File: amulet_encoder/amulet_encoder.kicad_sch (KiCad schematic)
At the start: 42 parts, among them J7 SM07B-GHS-TB, Q7 PMV90ENER, U1 MA732GQ, U2 SN74AHC1G02DBVR

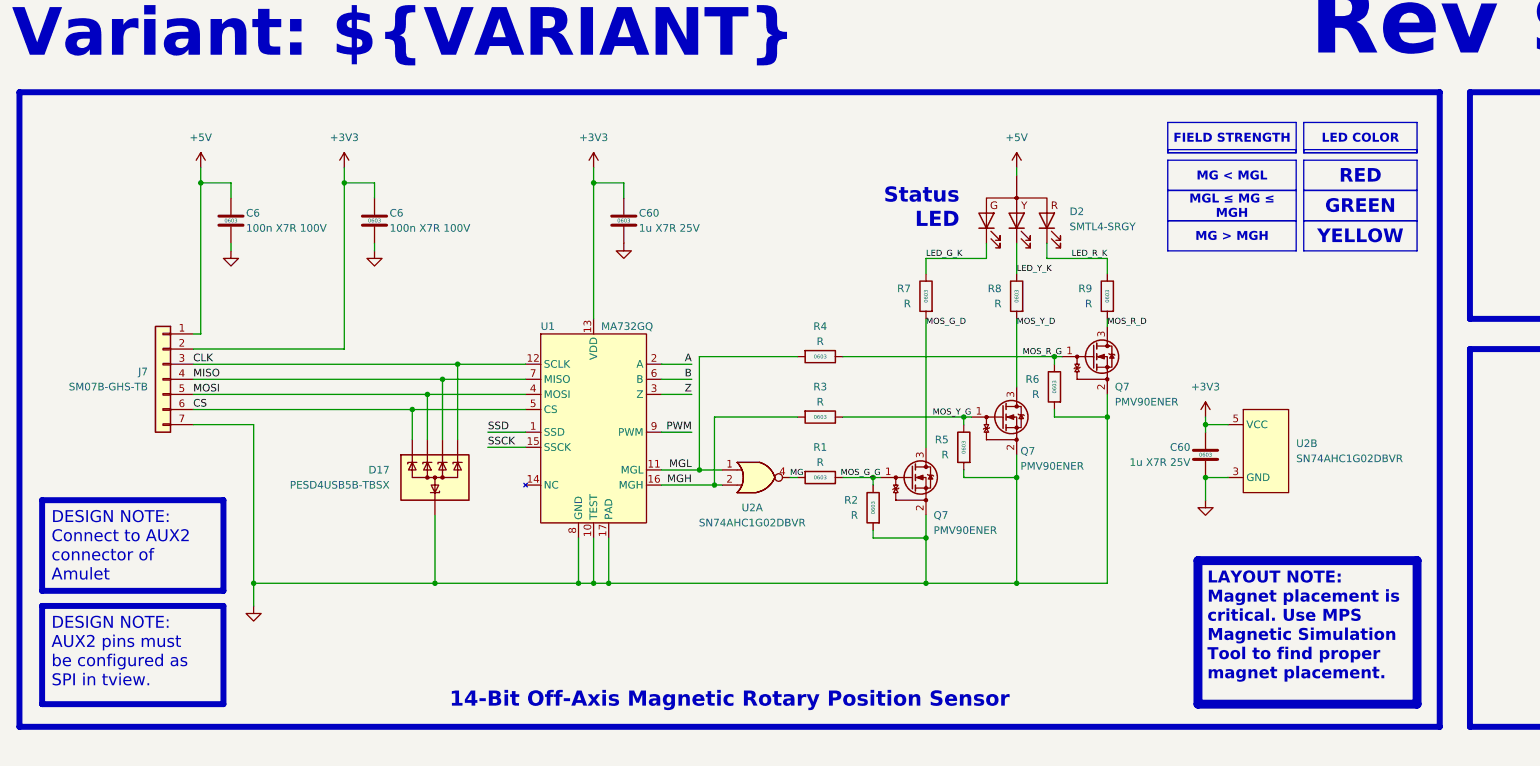
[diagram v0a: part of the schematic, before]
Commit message: preliminary layout
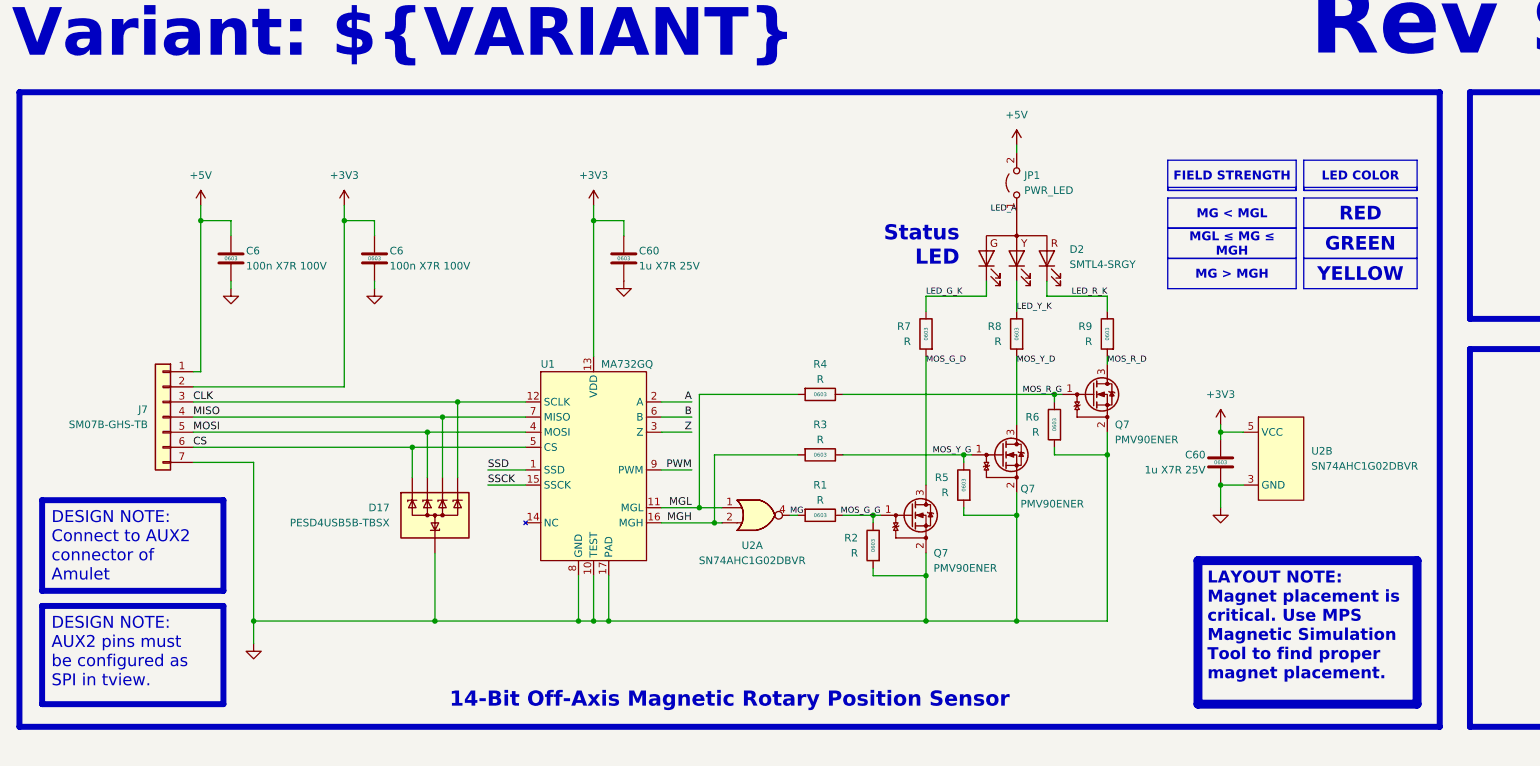
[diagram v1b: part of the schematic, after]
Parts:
- added JP1: PWR_LED, Jumper:SolderJumper-2_P1.3mm_Open_RoundedPad1.0x1.5mm, symbol Jumper:Jumper_2_Open
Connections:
- net +5V: now also JP1.2 (B); no longer D2.4 (A)
- new net LED_A: D2.4 (A), JP1.1 (A)
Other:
- moved on the sheet: C6, C60, D17, D2, J7, Q7, R1, R2, R3, R4, R5, R6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

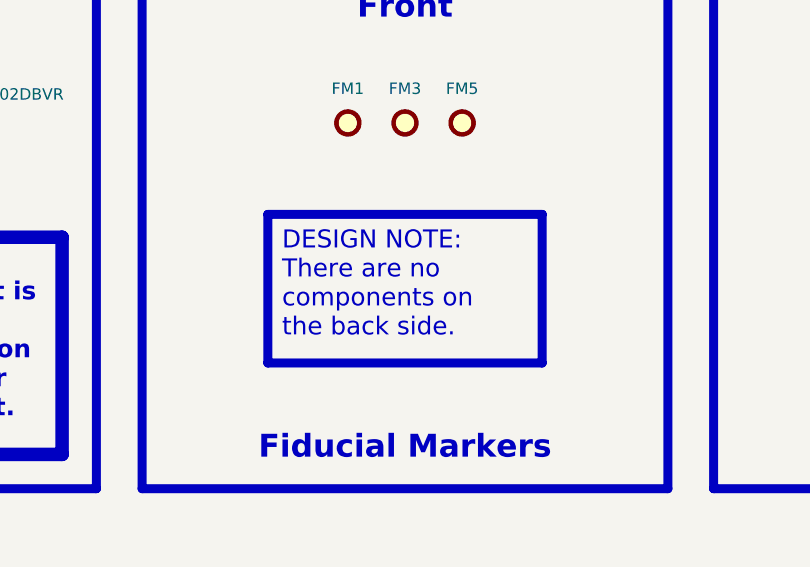
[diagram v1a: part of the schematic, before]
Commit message: preliminary routing of encoder
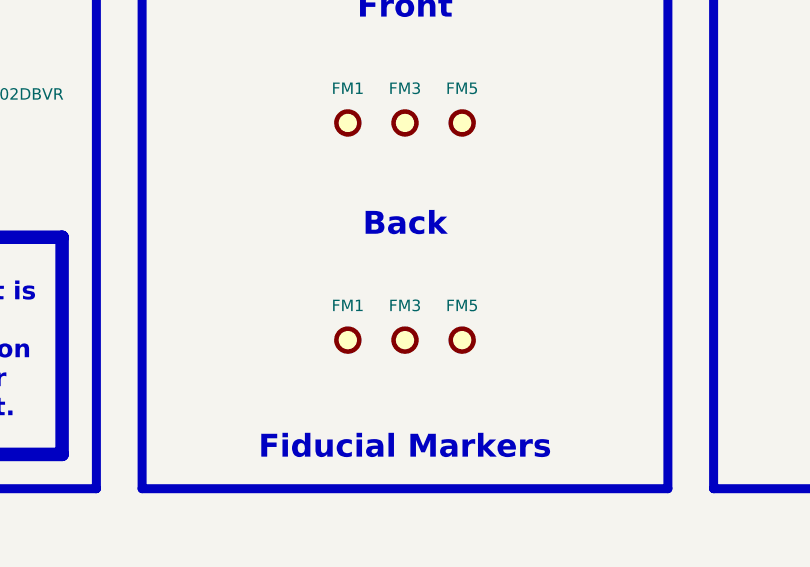
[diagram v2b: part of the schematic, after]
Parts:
- added FM1, FM3, FM5: Fiducial, 0_fiducials:Fiducial_1mm_Mask2mm, symbol Mechanical:Fiducial
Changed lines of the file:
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@@
     (fill (type none))
+  )
+  (text_box "Back"
+    (at 270.51 134.62 0) (size 58.42 9.525)
+    (stroke (width -0.0001) (type default))
+    (fill (type none))
+    (effects (font (face "Times New Roman") (size 2.54 2.54) (thickness 0.508) bold (color 0 0 0 1)) (justify bottom))
   )
   (text_box "RED"
@@
     (fill (type none))
     (effects (font (face "Times New Roman") (size 1.5 1.5) bold (color 0 0 127 1)))
-  )
-  (text_box "DESIGN NOTE:\nThere are no components on the back side."
-    (at 284.48 139.7 0) (size 30.48 16.51)
-    (stroke (width 1) (type solid) (color 200 200 200 1))
-    (fill (type none))
-    (effects (font (face "Arial") (size 2 2) (color 0 0 0 1)) (justify left top))
   )
   (text_box "GREEN"
@@
         (path "/7ccf8ada-fee6-4b84-aac5-5b2beb2f6969"
           (reference "TP3") (unit 1)
+        )
+      )
+    )
+  )
+  (symbol (lib_id "Mechanical:Fiducial") (at 293.37 153.67 0) (unit 1)
+    (in_bom no) (on_board yes) (dnp no)
+    (property "Reference" "FM1" (at 293.37 149.86 0)
+      (effects (font (size 1.27 1.27)))
+    )
+    (property "Value" "Fiducial" (at 295.91 154.94 0)
+      (effects (font (size 1.27 1.27)) (justify left) hide)
+    )
+    (property "Footprint" "0_fiducials:Fiducial_1mm_Mask2mm" (at 293.37 153.67 0)
+      (effects (font (size 1.27 1.27)) hide)
+    )
+    (property "Datasheet" "~" (at 293.37 153.67 0)
+      (effects (font (size 1.27 1.27)) hide)
+    )
+    (instances
+      (project "amulet_controller"
+        (path "/0650c7a8-acba-429c-9f8e-eec0baf0bc1c/fede4c36-00cc-4d3d-b71c-5243ba232202/c35a2394-f5db-4d2b-a6ba-34798059bc1f"
+          (reference "FM1") (unit 1)
+        )
+      )
+      (project "amulet_encoder"
+        (path "/7ccf8ada-fee6-4b84-aac5-5b2beb2f6969"
+          (reference "FM4") (unit 1)
+        )
+      )
+    )
+  )
+  (symbol (lib_id "Mechanical:Fiducial") (at 299.72 153.67 0) (unit 1)
+    (in_bom no) (on_board yes) (dnp no)
+    (property "Reference" "FM3" (at 299.72 149.86 0)
+      (effects (font (size 1.27 1.27)))
+    )
+    (property "Value" "Fiducial" (at 302.26 154.94 0)
+      (effects (font (size 1.27 1.27)) (justify left) hide)
+    )
+    (property "Footprint" "0_fiducials:Fiducial_1mm_Mask2mm" (at 299.72 153.67 0)
+      (effects (font (size 1.27 1.27)) hide)
+    )
+    (property "Datasheet" "~" (at 299.72 153.67 0)
+      (effects (font (size 1.27 1.27)) hide)
+    )
+    (instances
+      (project "amulet_controller"
+        (path "/0650c7a8-acba-429c-9f8e-eec0baf0bc1c/fede4c36-00cc-4d3d-b71c-5243ba232202/c35a2394-f5db-4d2b-a6ba-34798059bc1f"
+          (reference "FM3") (unit 1)
+        )
+      )
+      (project "amulet_encoder"
+        (path "/7ccf8ada-fee6-4b84-aac5-5b2beb2f6969"
+          (reference "FM5") (unit 1)
         )
       )
@@
         )
       )
+    )
+  )
+  (symbol (lib_id "Mechanical:Fiducial") (at 306.07 153.67 0) (unit 1)
+    (in_bom no) (on_board yes) (dnp no)
+    (property "Reference" "FM5" (at 306.07 149.86 0)
+      (effects (font (size 1.27 1.27)))
+    )
+    (property "Value" "Fiducial" (at 308.61 154.94 0)
+      (effects (font (size 1.27 1.27)) (justify left) hide)
+    )
+    (property "Footprint" "0_fiducials:Fiducial_1mm_Mask2mm" (at 306.07 153.67 0)
+      (effects (font (size 1.27 1.27)) hide)
+    )
+    (property "Datasheet" "~" (at 306.07 153.67 0)
+      (effects (font (size 1.27 1.27)) hide)
+    )
+    (instances
+      (project "amulet_controller"
+        (path "/0650c7a8-acba-429c-9f8e-eec0baf0bc1c/fede4c36-00cc-4d3d-b71c-5243ba232202/c35a2394-f5db-4d2b-a6ba-34798059bc1f"
+          (reference "FM5") (unit 1)
+        )
+      )
+      (project "amulet_encoder"
+        (path "/7ccf8ada-fee6-4b84-aac5-5b2beb2f6969"
+          (reference "FM6") (unit 1)
+        )
+      )

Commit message: rough version of encoder
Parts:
- C6: Manufacturer (none) -> Taiyo Yuden; Manufacturer Part Number (none) -> HMK107B7104KAHT; Supplier 1 (none) -> Digikey; Supplier Part Number 1 (none) -> 587-6009-1-ND
- D2: Supplier 1 (none) -> Digikey; Supplier Part Number 1 (none) -> 492-2193-1-ND
- JP1: now left out of the parts list
- R1, R3, R4: value R -> 1k 1/10W 1%; Manufacturer (none) -> YAGEO; Manufacturer Part Number (none) -> RC0603FR-071KL; Supplier 1 (none) -> Digikey; Supplier Part Number 1 (none) -> 311-1.00KHRCT-ND
- R2, R5, R6: value R -> 100k 1/10W 1%; Manufacturer (none) -> YAGEO; Manufacturer Part Number (none) -> RC0603FR-07100KL; Supplier 1 (none) -> Digikey; Supplier Part Number 1 (none) -> 311-100KHRCT-ND
- R7: value R -> 200R 1/5W 1%; Manufacturer (none) -> YAGEO; Manufacturer Part Number (none) -> AC0603FR-7W200RL; Supplier 1 (none) -> Digikey; Supplier Part Number 1 (none) -> 13-AC0603FR-7W200RLCT-ND
- R8, R9: value R -> 330R 1/5W 1%; Manufacturer (none) -> TE Connectivity Passive Product; Manufacturer Part Number (none) -> CRGH0603F330R; Supplier 1 (none) -> Digikey; Supplier Part Number 1 (none) -> A129541CT-ND
- TP1: footprint 0_testpoint:TestPoint_Pad_D1mm_Front -> 0_testpoint:TestPoint_Pad_D1mm_THT
- U1: Supplier 1 (none) -> Digikey; Supplier Part Number 1 (none) -> 1589-MA732GQ-ZCT-ND
- U2: Manufacturer (none) -> Texas Instruments; Manufacturer  Texas Instruments -> (none); Supplier 1 (none) -> Digikey; Supplier Part Number 1 (none) -> 296-1088-1-ND
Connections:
- net MG: now also R2.1
- net MGH: now also R5.1
- net MGL: now also R6.1
- net MOS_G_G: no longer R2.1
- net MOS_R_G: no longer R6.1
- net MOS_Y_G: no longer R5.1
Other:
- moved on the sheet: C6, C60, D17, D2, J7, JP1, Q7, R1, R2, R3, R4, R5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
